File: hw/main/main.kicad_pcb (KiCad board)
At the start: 2 copper layers, 50 x 50 mm, 22 parts, among them U1 MCP1703A-3302, U2 STM32L011D3, X1 01x04_P2.54mm_Hor, X2 01x04_P2.54mm_Hor

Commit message: wip
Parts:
- moved C1 50.5 mm to (199.2, 102.5)
- moved C2 50.5 mm to (192.9, 102.5)
- moved C3 50.5 mm to (190.3, 102.5)
- moved C4 50.5 mm to (181.3, 115.7)
- moved C5 50.5 mm to (205.6, 102.5)
- moved C6 50.5 mm to (183.4, 107.9)
- moved C8 50.5 mm to (184.6, 99.3)
- moved D1 50.5 mm to (213.2, 102.5)
- moved D3 50.5 mm to (188.4, 96.8)
- moved R1 50.5 mm to (181.4, 112.6)
- moved R2 50.5 mm to (210.7, 102.5)
- moved R3 50.5 mm to (208.1, 102.5)
- moved R4 50.5 mm to (189.1, 113.3)
- moved R7 50.5 mm to (184.6, 96.8)
- moved U1 50.5 mm to (196.1, 102.5)
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
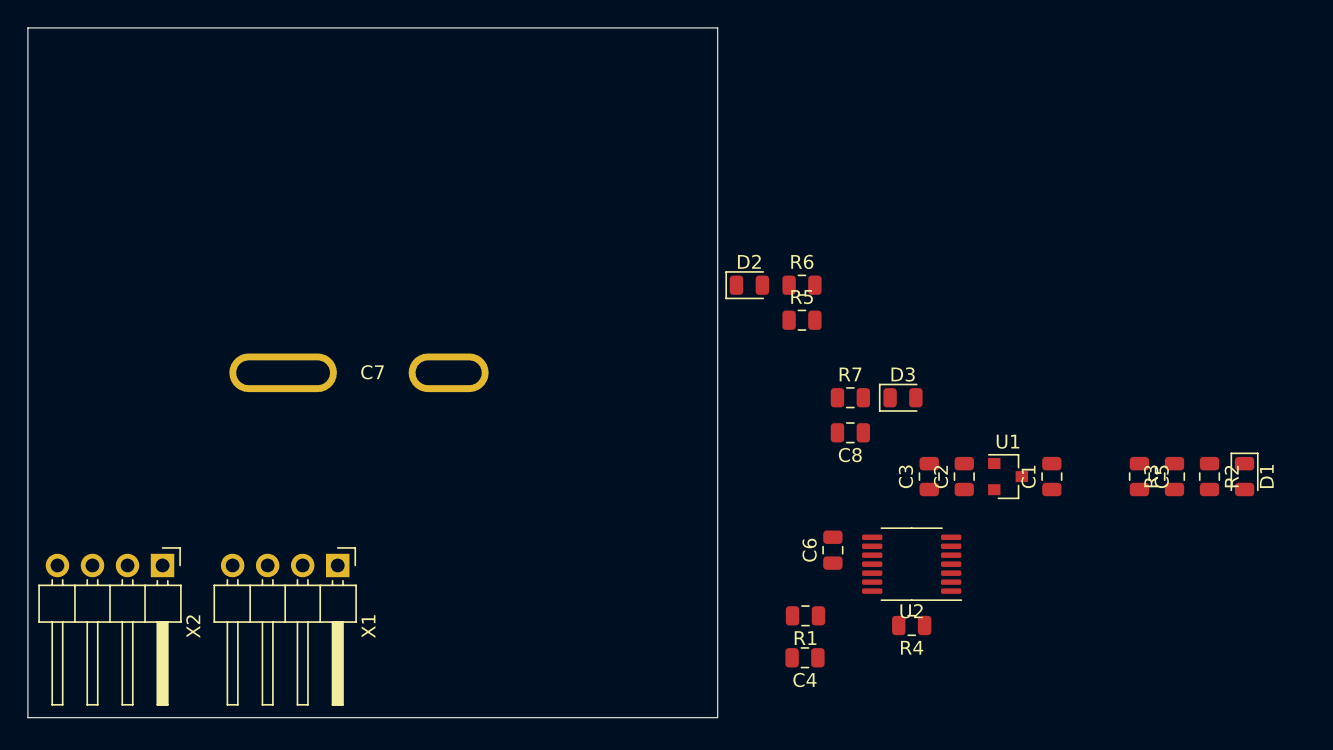
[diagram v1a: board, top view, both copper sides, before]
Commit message: Added timer 555 to measure sensor capacity
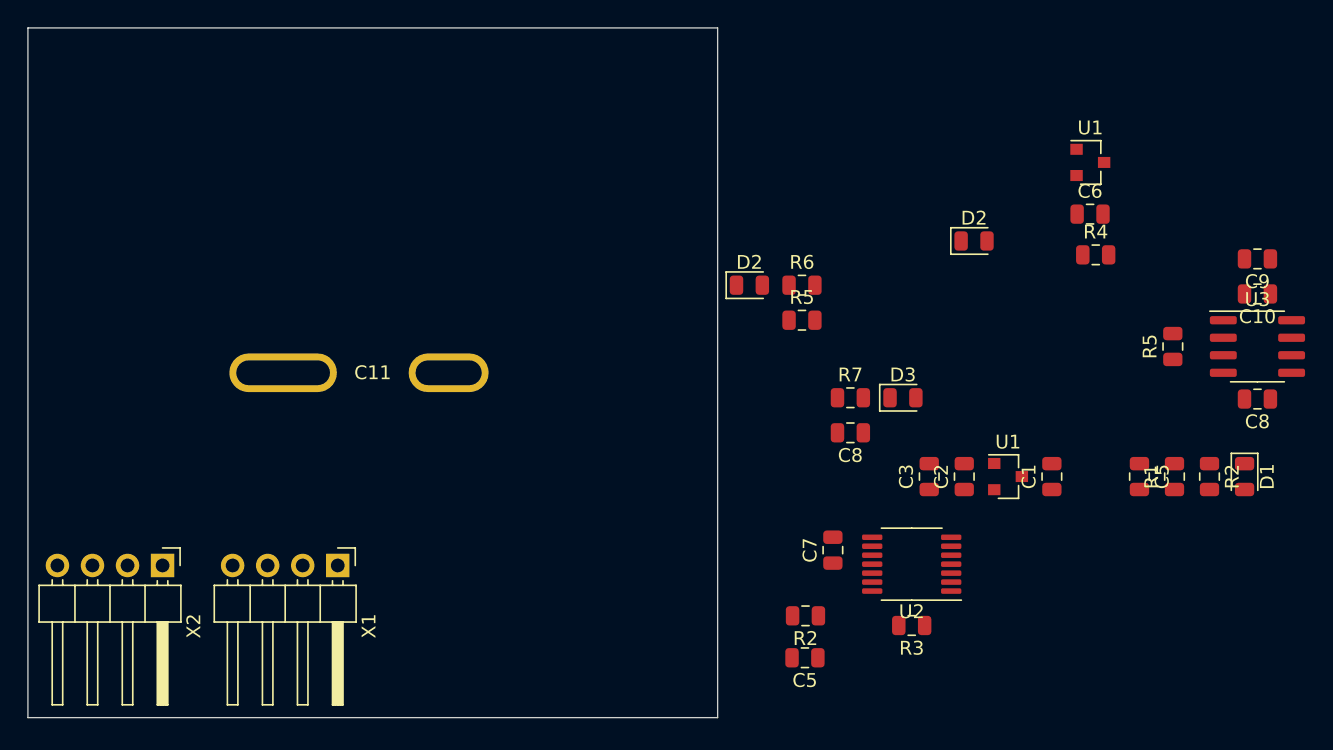
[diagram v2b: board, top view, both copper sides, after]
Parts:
- added C10: 100n_50V, Capacitor_SMD:C_0805_2012Metric, F.Cu at (214.1, 89.3)
- added C6: 10u_16V, Capacitor_SMD:C_0805_2012Metric, F.Cu at (202.0, 83.5)
- added C8: 100n_50V, Capacitor_SMD:C_0805_2012Metric, F.Cu at (214.1, 96.9)
- added C9: 10u_16V, Capacitor_SMD:C_0805_2012Metric, F.Cu at (214.1, 86.7)
- added D2: SS14HE, Diode_SMD:D_0805_2012Metric, F.Cu at (193.6, 85.4)
- added R4: 100K, Resistor_SMD:R_0805_2012Metric, F.Cu at (202.4, 86.5)
- added R5: 100K, Resistor_SMD:R_0805_2012Metric, F.Cu at (208.0, 93.1)
- added U1: MCP1703A-1802, Package_TO_SOT_SMD:SOT-23, F.Cu at (202.0, 79.8)
- added U3: LMC555xM, Package_SO:SOIC-8_3.9x4.9mm_P1.27mm, F.Cu at (214.1, 93.1)
- renumbered C7 to C11, C4 to C5, C6 to C7, R3 to R1, R1 to R2, R4 to R3
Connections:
- C11 pad 1: Net-(C7-Pad1) -> /Vsens
- D1 pad 2: /Vext -> Net-(D1-Pad2)
- R1 pad 2: /GPIO_EXTI15 -> /LPUART1_RX
- U2 pad 3: /GPIO_EXTI15 -> Net-(U2-Pad3)
- X2 pad 1: /Vext -> Net-(D1-Pad2)
